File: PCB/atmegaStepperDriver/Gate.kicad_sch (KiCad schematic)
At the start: 8 parts, among them Q18 TIP42C, Q19 BC557, Q20 BC547, Q21 TIP41C

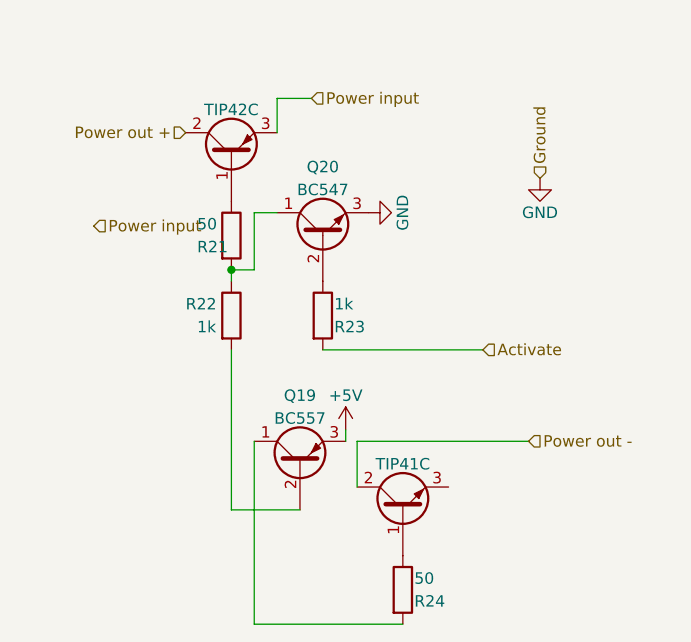
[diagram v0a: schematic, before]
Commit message: Fix gate; added termistor; gate sheet added; v0.8.4
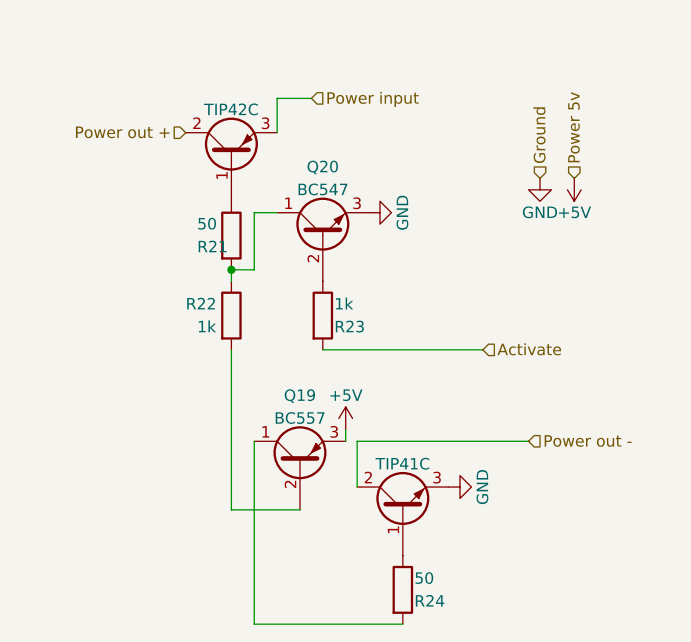
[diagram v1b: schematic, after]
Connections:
- net GND: now also Q21.3 (E)
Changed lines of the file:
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@@
     (effects (font (size 1.27 1.27)) (justify left))
   )
-  (hierarchical_label "Power input" (shape input) (at 92.6572 87.8452 0) (fields_autoplaced)
+  (hierarchical_label "Power 5v" (shape input) (at 146.05 82.55 90) (fields_autoplaced)
     (effects (font (size 1.27 1.27)) (justify left))
   )
@@
     (effects (font (size 1.27 1.27)) (justify left))
   )
+  (symbol (lib_id "power:+5V") (at 146.05 82.55 180) (unit 1)
+    (in_bom yes) (on_board yes) (dnp no)
+    (property "Reference" "#PWR033" (at 146.05 78.74 0)
+      (effects (font (size 1.27 1.27)) hide)
+    )
+    (property "Value" "+5V" (at 146.05 86.36 0)
+      (effects (font (size 1.27 1.27)))
+    )
+    (property "Footprint" "" (at 146.05 82.55 0)
+      (effects (font (size 1.27 1.27)) hide)
+    )
+    (property "Datasheet" "" (at 146.05 82.55 0)
+      (effects (font (size 1.27 1.27)) hide)
+    )
+    (pin "1")
+    (instances
+      (project "atmegaStepperDriver"
+        (path "/c84e7e69-c1fd-4499-93bc-6ad0c4ebade1/50d10c8e-db41-49f6-876e-74ecf5bb7f1a"
+          (reference "#PWR033") (unit 1)
+        )
+        (path "/c84e7e69-c1fd-4499-93bc-6ad0c4ebade1/2ed833cf-10fa-4bde-810e-ad6d3427afac"
+          (reference "#PWR036") (unit 1)
+        )
+        (path "/c84e7e69-c1fd-4499-93bc-6ad0c4ebade1/f39905cc-c290-436c-aa2b-a9f03eefcfde"
+          (reference "#PWR042") (unit 1)
+        )
+        (path "/c84e7e69-c1fd-4499-93bc-6ad0c4ebade1/62d8831a-46d2-48a9-80d1-37d529f4e814"
+          (reference "#PWR047") (unit 1)
+        )
+      )
+    )
+  )
   (symbol (lib_id "power:GND") (at 142.24 82.55 0) (unit 1)
     (in_bom yes) (on_board yes) (dnp no)
@@
         (path "/c84e7e69-c1fd-4499-93bc-6ad0c4ebade1/50d10c8e-db41-49f6-876e-74ecf5bb7f1a"
           (reference "#PWR032") (unit 1)
+        )
+        (path "/c84e7e69-c1fd-4499-93bc-6ad0c4ebade1/2ed833cf-10fa-4bde-810e-ad6d3427afac"
+          (reference "#PWR035") (unit 1)
+        )
+        (path "/c84e7e69-c1fd-4499-93bc-6ad0c4ebade1/f39905cc-c290-436c-aa2b-a9f03eefcfde"
+          (reference "#PWR041") (unit 1)
+        )
+        (path "/c84e7e69-c1fd-4499-93bc-6ad0c4ebade1/62d8831a-46d2-48a9-80d1-37d529f4e814"
+          (reference "#PWR046") (unit 1)
         )
       )
@@
           (reference "Q18") (unit 1)
         )
+        (path "/c84e7e69-c1fd-4499-93bc-6ad0c4ebade1/2ed833cf-10fa-4bde-810e-ad6d3427afac"
+          (reference "Q1") (unit 1)
+        )
+        (path "/c84e7e69-c1fd-4499-93bc-6ad0c4ebade1/f39905cc-c290-436c-aa2b-a9f03eefcfde"
+          (reference "Q5") (unit 1)
+        )
+        (path "/c84e7e69-c1fd-4499-93bc-6ad0c4ebade1/62d8831a-46d2-48a9-80d1-37d529f4e814"
+          (reference "Q9") (unit 1)
+        )
       )
     )
@@
           (reference "Q19") (unit 1)
         )
+        (path "/c84e7e69-c1fd-4499-93bc-6ad0c4ebade1/2ed833cf-10fa-4bde-810e-ad6d3427afac"
+          (reference "Q2") (unit 1)
+        )
+        (path "/c84e7e69-c1fd-4499-93bc-6ad0c4ebade1/f39905cc-c290-436c-aa2b-a9f03eefcfde"
+          (reference "Q6") (unit 1)
+        )
+        (path "/c84e7e69-c1fd-4499-93bc-6ad0c4ebade1/62d8831a-46d2-48a9-80d1-37d529f4e814"
+          (reference "Q10") (unit 1)
+        )
       )
     )
@@
           (reference "R22") (unit 1)
         )
+        (path "/c84e7e69-c1fd-4499-93bc-6ad0c4ebade1/2ed833cf-10fa-4bde-810e-ad6d3427afac"
+          (reference "R4") (unit 1)
+        )
+        (path "/c84e7e69-c1fd-4499-93bc-6ad0c4ebade1/f39905cc-c290-436c-aa2b-a9f03eefcfde"
+          (reference "R8") (unit 1)
+        )
+        (path "/c84e7e69-c1fd-4499-93bc-6ad0c4ebade1/62d8831a-46d2-48a9-80d1-37d529f4e814"
+          (reference "R12") (unit 1)
+        )
       )
     )
@@
           (reference "R23") (unit 1)
         )
+        (path "/c84e7e69-c1fd-4499-93bc-6ad0c4ebade1/2ed833cf-10fa-4bde-810e-ad6d3427afac"
+          (reference "R5") (unit 1)
+        )
+        (path "/c84e7e69-c1fd-4499-93bc-6ad0c4ebade1/f39905cc-c290-436c-aa2b-a9f03eefcfde"
+          (reference "R9") (unit 1)
+        )
+        (path "/c84e7e69-c1fd-4499-93bc-6ad0c4ebade1/62d8831a-46d2-48a9-80d1-37d529f4e814"
+          (reference "R13") (unit 1)
+        )
+      )
+    )
+  )
+  (symbol (lib_id "power:GND") (at 132.08 116.84 90) (unit 1)
+    (in_bom yes) (on_board yes) (dnp no)
+    (property "Reference" "#PWR040" (at 138.43 116.84 0)
+      (effects (font (size 1.27 1.27)) hide)
+    )
+    (property "Value" "GND" (at 135.89 116.84 0)
+      (effects (font (size 1.27 1.27)))
+    )
+    (property "Footprint" "" (at 132.08 116.84 0)
+      (effects (font (size 1.27 1.27)) hide)
+    )
+    (property "Datasheet" "" (at 132.08 116.84 0)
+      (effects (font (size 1.27 1.27)) hide)
+    )
+    (pin "1")
+    (instances
+      (project "atmegaStepperDriver"
+        (path "/c84e7e69-c1fd-4499-93bc-6ad0c4ebade1/50d10c8e-db41-49f6-876e-74ecf5bb7f1a"
+          (reference "#PWR040") (unit 1)
+        )
+        (path "/c84e7e69-c1fd-4499-93bc-6ad0c4ebade1/2ed833cf-10fa-4bde-810e-ad6d3427afac"
+          (reference "#PWR034") (unit 1)
+        )
+        (path "/c84e7e69-c1fd-4499-93bc-6ad0c4ebade1/f39905cc-c290-436c-aa2b-a9f03eefcfde"
+          (reference "#PWR039") (unit 1)
+        )
+        (path "/c84e7e69-c1fd-4499-93bc-6ad0c4ebade1/62d8831a-46d2-48a9-80d1-37d529f4e814"
+          (reference "#PWR045") (unit 1)
+        )
       )
     )
@@
         (path "/c84e7e69-c1fd-4499-93bc-6ad0c4ebade1/50d10c8e-db41-49f6-876e-74ecf5bb7f1a"
           (reference "R24") (unit 1)
+        )
+        (path "/c84e7e69-c1fd-4499-93bc-6ad0c4ebade1/2ed833cf-10fa-4bde-810e-ad6d3427afac"
+          (reference "R6") (unit 1)
+        )
+        (path "/c84e7e69-c1fd-4499-93bc-6ad0c4ebade1/f39905cc-c290-436c-aa2b-a9f03eefcfde"
+          (reference "R10") (unit 1)
+        )
+        (path "/c84e7e69-c1fd-4499-93bc-6ad0c4ebade1/62d8831a-46d2-48a9-80d1-37d529f4e814"
+          (reference "R14") (unit 1)
         )
       )
@@
           (reference "Q21") (unit 1)
         )
+        (path "/c84e7e69-c1fd-4499-93bc-6ad0c4ebade1/2ed833cf-10fa-4bde-810e-ad6d3427afac"
+          (reference "Q4") (unit 1)
+        )
+        (path "/c84e7e69-c1fd-4499-93bc-6ad0c4ebade1/f39905cc-c290-436c-aa2b-a9f03eefcfde"
+          (reference "Q8") (unit 1)
+        )
+        (path "/c84e7e69-c1fd-4499-93bc-6ad0c4ebade1/62d8831a-46d2-48a9-80d1-37d529f4e814"
+          (reference "Q12") (unit 1)
+        )
       )
     )
@@
           (reference "#PWR030") (unit 1)
         )
+        (path "/c84e7e69-c1fd-4499-93bc-6ad0c4ebade1/2ed833cf-10fa-4bde-810e-ad6d3427afac"
+          (reference "#PWR017") (unit 1)
+        )
+        (path "/c84e7e69-c1fd-4499-93bc-6ad0c4ebade1/f39905cc-c290-436c-aa2b-a9f03eefcfde"
+          (reference "#PWR037") (unit 1)
+        )
+        (path "/c84e7e69-c1fd-4499-93bc-6ad0c4ebade1/62d8831a-46d2-48a9-80d1-37d529f4e814"
+          (reference "#PWR043") (unit 1)
+        )
       )
     )
@@
           (reference "R21") (unit 1)
         )
+        (path "/c84e7e69-c1fd-4499-93bc-6ad0c4ebade1/2ed833cf-10fa-4bde-810e-ad6d3427afac"
+          (reference "R3") (unit 1)
+        )
+        (path "/c84e7e69-c1fd-4499-93bc-6ad0c4ebade1/f39905cc-c290-436c-aa2b-a9f03eefcfde"
+          (reference "R7") (unit 1)
+        )
+        (path "/c84e7e69-c1fd-4499-93bc-6ad0c4ebade1/62d8831a-46d2-48a9-80d1-37d529f4e814"
+          (reference "R11") (unit 1)
+        )
       )
     )
@@
         (path "/c84e7e69-c1fd-4499-93bc-6ad0c4ebade1/50d10c8e-db41-49f6-876e-74ecf5bb7f1a"
           (reference "#PWR031") (unit 1)
+        )
+        (path "/c84e7e69-c1fd-4499-93bc-6ad0c4ebade1/2ed833cf-10fa-4bde-810e-ad6d3427afac"
+          (reference "#PWR019") (unit 1)
+        )
+        (path "/c84e7e69-c1fd-4499-93bc-6ad0c4ebade1/f39905cc-c290-436c-aa2b-a9f03eefcfde"
+          (reference "#PWR038") (unit 1)
+        )
+        (path "/c84e7e69-c1fd-4499-93bc-6ad0c4ebade1/62d8831a-46d2-48a9-80d1-37d529f4e814"
+          (reference "#PWR044") (unit 1)
         )
       )
@@
           (reference "Q20") (unit 1)
         )
-      )
+        (path "/c84e7e69-c1fd-4499-93bc-6ad0c4ebade1/2ed833cf-10fa-4bde-810e-ad6d3427afac"
+          (reference "Q3") (unit 1)
+        )
+        (path "/c84e7e69-c1fd-4499-93bc-6ad0c4ebade1/f39905cc-c290-436c-aa2b-a9f03eefcfde"
+          (reference "Q7") (unit 1)
+        )
+        (path "/c84e7e69-c1fd-4499-93bc-6ad0c4ebade1/62d8831a-46d2-48a9-80d1-37d529f4e814"
+          (reference "Q11") (unit 1)
+        )
+      )

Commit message: someData; idk what i did, forgot to push it
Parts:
- added D16, D8: D, Diode_THT:D_DO-35_SOD27_P10.16mm_Horizontal, symbol Device:D
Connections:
- net GND: now also D8.2 (A)
- net Power input: now also D16.1 (K)
- net Power out +: now also D16.2 (A)
- net Power out -: now also D8.1 (K)
- net +5V renamed Power 5v
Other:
- title: (none) -> atmegaStepperDriver Developer board
